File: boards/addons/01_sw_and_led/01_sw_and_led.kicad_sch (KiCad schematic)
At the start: 0 parts

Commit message: 回路図書いて FP 割り当て
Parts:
- added D1, D2: LED, LED_THT:LED_D5.0mm, symbol Device:LED
- added R1, R2, R3, R4: R, Resistor_THT:R_Axial_DIN0207_L6.3mm_D2.5mm_P10.16mm_Horizontal, symbol Device:R
- added SW1, SW2: SW_Push, Button_Switch_THT:SW_PUSH-12mm, symbol Switch:SW_Push
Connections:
- new net: D1.2 (A), R3.2
- new net: D2.2 (A), R4.2
- new net +3.3V: R1.1, R2.1
- new net GND: D1.1 (K), D2.1 (K), SW1.2, SW2.2
- new net LED1: R3.1
- new net LED2: R4.1
- new net SW1: R1.2, SW1.1
- new net SW2: R2.2, SW2.1

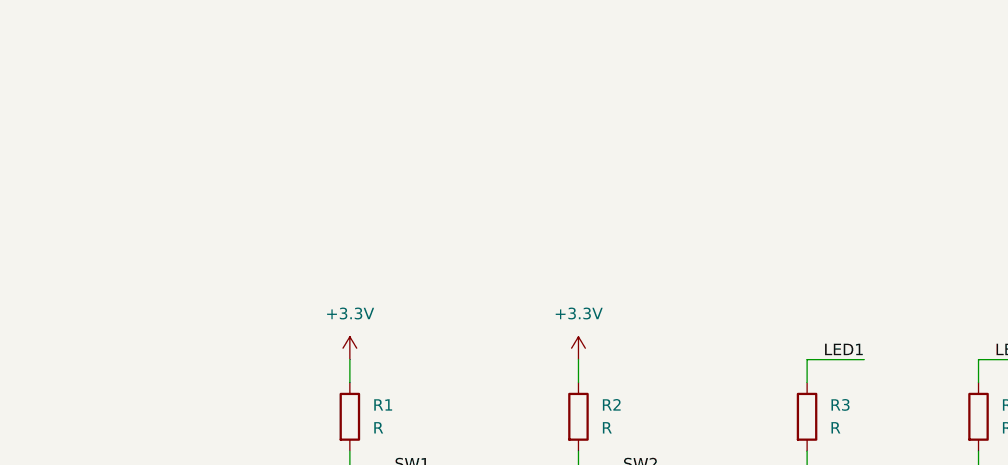
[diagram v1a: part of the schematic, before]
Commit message: 電源と入出力のピンソケット追加
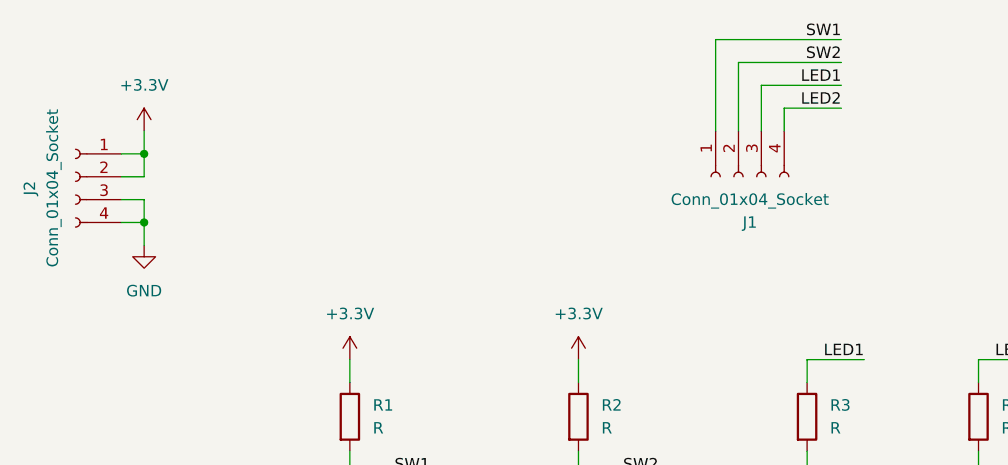
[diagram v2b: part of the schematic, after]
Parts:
- added J1, J2: Conn_01x04_Socket, Connector_PinSocket_2.54mm:PinSocket_1x04_P2.54mm_Vertical, symbol Connector:Conn_01x04_Socket
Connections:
- net +3.3V: now also J2.1 (Pin_1), J2.2 (Pin_2)
- net GND: now also J2.3 (Pin_3), J2.4 (Pin_4)
- net LED1: now also J1.3 (Pin_3)
- net LED2: now also J1.4 (Pin_4)
- net SW1: now also J1.1 (Pin_1)
- net SW2: now also J1.2 (Pin_2)

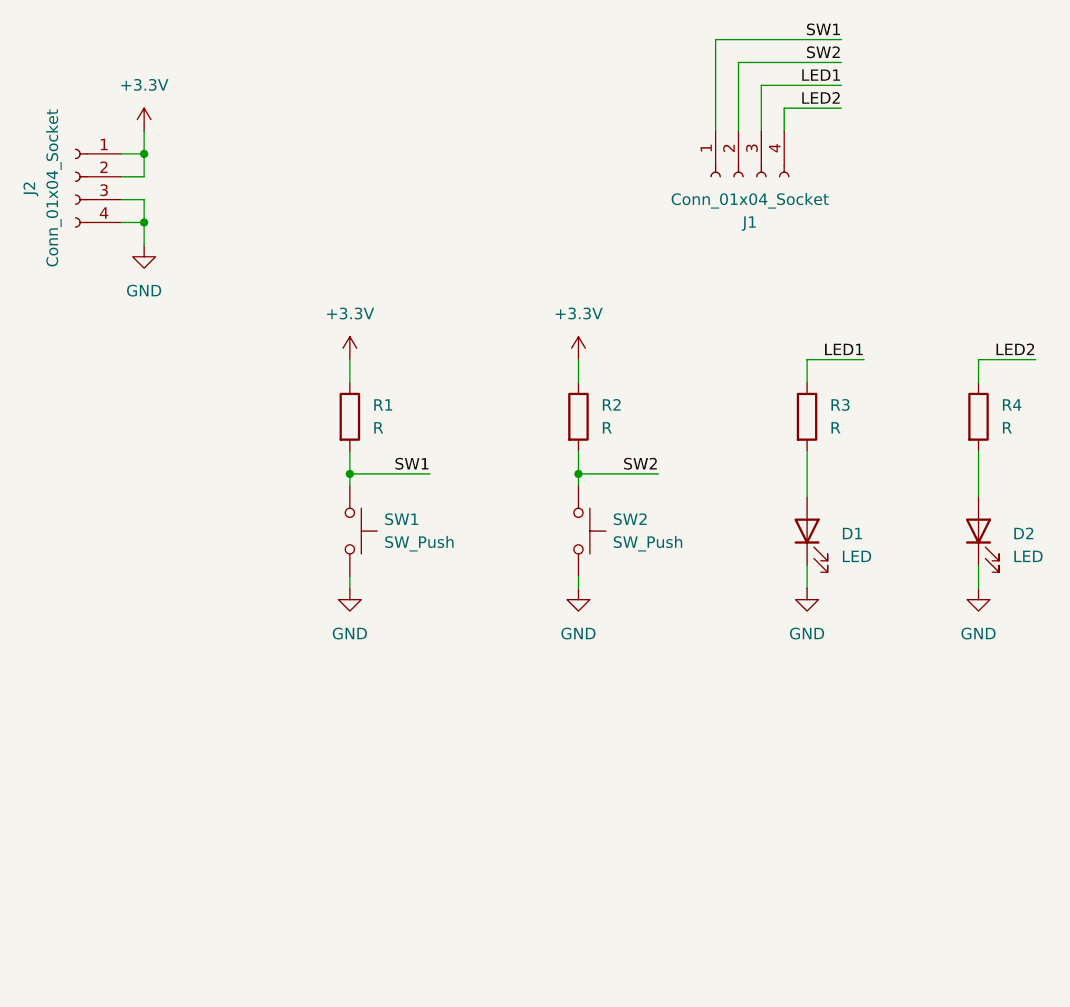
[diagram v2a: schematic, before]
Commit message: スイッチのプルアップ抵抗はなくしました
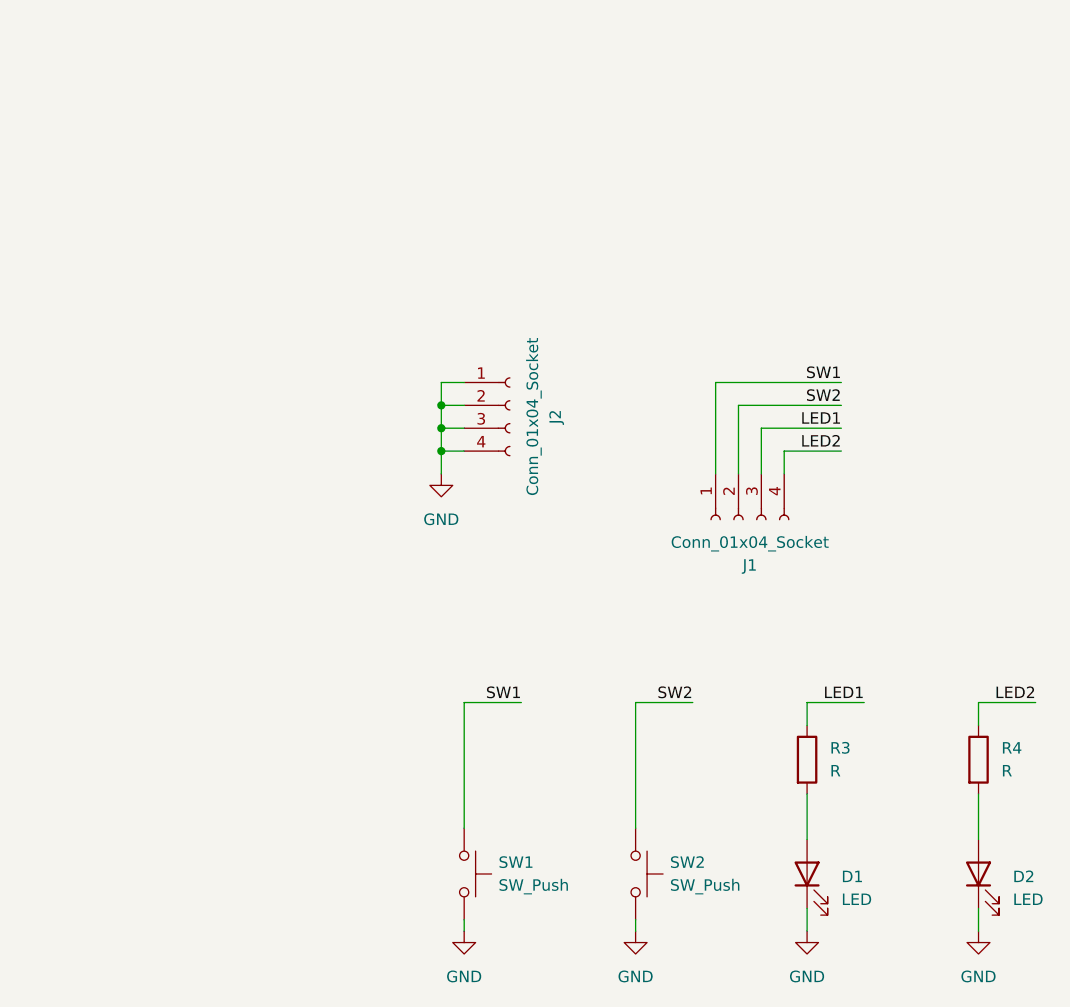
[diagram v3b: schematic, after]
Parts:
- removed R1, R2: R, Resistor_THT:R_Axial_DIN0207_L6.3mm_D2.5mm_P10.16mm_Horizontal, symbol Device:R
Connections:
- net +3.3V is gone; now on net GND: J2.1 (Pin_1), J2.2 (Pin_2)
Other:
- moved on the sheet: D1, D2, J1, R3, R4, SW1, SW2

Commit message: ナンバリング修正
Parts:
- renumbered R3 to R1, R4 to R2
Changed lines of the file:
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@@
 		(dnp no)
 		(fields_autoplaced yes)
-		(property "Reference" "#PWR04"
+		(property "Reference" "#PWR03"
 			(at 133.35 133.35 0)
 			(effects
@@
 			(project "01_sw_and_led"
 				(path "/20fd3bc1-be81-458c-a006-fb35973ca7f8"
-					(reference "#PWR04")
+					(reference "#PWR03")
 					(unit 1)
 				)
@@
 		(dnp no)
 		(fields_autoplaced yes)
-		(property "Reference" "#PWR06"
+		(property "Reference" "#PWR05"
 			(at 171.45 133.35 0)
 			(effects
@@
 			(project "01_sw_and_led"
 				(path "/20fd3bc1-be81-458c-a006-fb35973ca7f8"
-					(reference "#PWR06")
+					(reference "#PWR05")
 					(unit 1)
 				)
@@
 		(dnp no)
 		(fields_autoplaced yes)
-		(property "Reference" "R4"
+		(property "Reference" "R2"
 			(at 173.99 106.6799 0)
 			(effects
@@
 			(project "01_sw_and_led"
 				(path "/20fd3bc1-be81-458c-a006-fb35973ca7f8"
-					(reference "R4")
+					(reference "R2")
 					(unit 1)
 				)
@@
 		(dnp no)
 		(fields_autoplaced yes)
-		(property "Reference" "#PWR02"
+		(property "Reference" "#PWR01"
 			(at 111.76 82.55 0)
 			(effects
@@
 			(project "01_sw_and_led"
 				(path "/20fd3bc1-be81-458c-a006-fb35973ca7f8"
-					(reference "#PWR02")
+					(reference "#PWR01")
 					(unit 1)
 				)
@@
 		(dnp no)
 		(fields_autoplaced yes)
-		(property "Reference" "#PWR05"
+		(property "Reference" "#PWR04"
 			(at 152.4 133.35 0)
 			(effects
@@
 			(project "01_sw_and_led"
 				(path "/20fd3bc1-be81-458c-a006-fb35973ca7f8"
-					(reference "#PWR05")
+					(reference "#PWR04")
 					(unit 1)
 				)
@@
 		(dnp no)
 		(fields_autoplaced yes)
-		(property "Reference" "#PWR01"
+		(property "Reference" "#PWR02"
 			(at 114.3 133.35 0)
 			(effects
@@
 			(project ""
 				(path "/20fd3bc1-be81-458c-a006-fb35973ca7f8"
-					(reference "#PWR01")
+					(reference "#PWR02")
 					(unit 1)
 				)
@@
 		(dnp no)
 		(fields_autoplaced yes)
-		(property "Reference" "R3"
+		(property "Reference" "R1"
 			(at 154.94 106.6799 0)
 			(effects
@@
 			(project "01_sw_and_led"
 				(path "/20fd3bc1-be81-458c-a006-fb35973ca7f8"
-					(reference "R3")
-					(unit 1)
-				)
+					(reference "R1")
+					(unit 1)
+				)
